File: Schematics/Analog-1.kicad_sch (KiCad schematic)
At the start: 65 parts, among them U23 TCA9548A, U24 MCP4728, U25 MCP4728, U26 MCP4728, U27 MCP4728, U28 MCP4728, U29 MCP4728, U30 MCP4728, U31 MCP4728, U32 MCP4728, U33 MCP4728, U34 MCP4728, U35 MCP4728, U36 MCP4728, U37 MCP4728, U38 MCP4728, U39 MCP4728, U40 TCA9548A, U41 LM1117-3.3, U42 MCP4728, U43 MCP4728, U44 MCP4728, U45 MCP4728, U46 MCP4728, U47 MCP4728, U48 TCA9548A

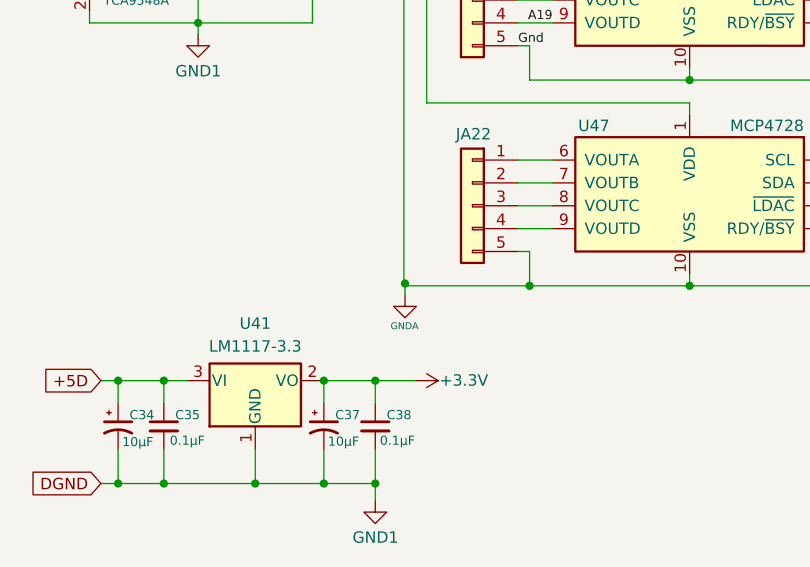
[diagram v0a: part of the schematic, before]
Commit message: Now with dual ESP32 with Midi32 and Disp32.
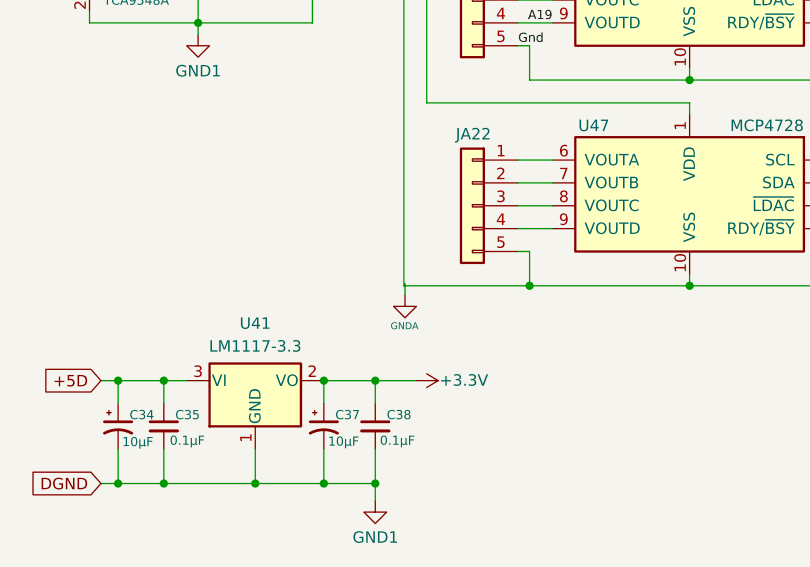
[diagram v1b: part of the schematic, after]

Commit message: Disp32 interface working properly.
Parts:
- renumbered R11 to R10, R5 to R4, R6 to R5, R7 to R6, R8 to R7, R9 to R8, R10 to R9
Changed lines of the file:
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@@
   (symbol (lib_id "Device:R_Small_US") (at 205.74 86.36 0) (mirror y) (unit 1)
     (in_bom yes) (on_board yes) (dnp no)
-    (property "Reference" "R6" (at 209.9411 84.455 0)
+    (property "Reference" "R5" (at 209.9411 84.455 0)
       (effects (font (size 1.016 1.016)) (justify left))
     )
@@
       (project "Schematics-Midi32"
         (path "/718f017d-28fe-4e29-b548-40db8e21cec7/5bc16b3a-a1cd-4002-8881-eefa1f194921"
-          (reference "R6") (unit 1)
+          (reference "R5") (unit 1)
         )
       )
@@
   (symbol (lib_id "Device:R_Small_US") (at 208.28 69.85 0) (mirror y) (unit 1)
     (in_bom yes) (on_board yes) (dnp no)
-    (property "Reference" "R7" (at 208.3796 67.9875 0)
+    (property "Reference" "R6" (at 208.3796 67.9875 0)
       (effects (font (size 1.016 1.016)) (justify right))
     )
@@
       (project "Schematics-Midi32"
         (path "/718f017d-28fe-4e29-b548-40db8e21cec7/5bc16b3a-a1cd-4002-8881-eefa1f194921"
-          (reference "R7") (unit 1)
+          (reference "R6") (unit 1)
         )
       )
@@
   (symbol (lib_id "Device:R_Small_US") (at 24.13 71.12 0) (unit 1)
     (in_bom yes) (on_board yes) (dnp no)
-    (property "Reference" "R5" (at 18.8695 69.2735 0)
+    (property "Reference" "R4" (at 18.8695 69.2735 0)
       (effects (font (size 1.27 1.27)) (justify left))
     )
@@
       (project "Schematics-Midi32"
         (path "/718f017d-28fe-4e29-b548-40db8e21cec7/5bc16b3a-a1cd-4002-8881-eefa1f194921"
-          (reference "R5") (unit 1)
+          (reference "R4") (unit 1)
         )
       )
@@
   (symbol (lib_id "Device:R_Small_US") (at 317.5 69.85 0) (mirror y) (unit 1)
     (in_bom yes) (on_board yes) (dnp no)
-    (property "Reference" "R10" (at 317.7079 67.884 0)
+    (property "Reference" "R9" (at 317.7079 67.884 0)
       (effects (font (size 1.016 1.016)) (justify right))
     )
@@
       (project "Schematics-Midi32"
         (path "/718f017d-28fe-4e29-b548-40db8e21cec7/5bc16b3a-a1cd-4002-8881-eefa1f194921"
-          (reference "R10") (unit 1)
+          (reference "R9") (unit 1)
         )
       )
@@
   (symbol (lib_id "Device:R_Small_US") (at 213.995 69.85 0) (mirror y) (unit 1)
     (in_bom yes) (on_board yes) (dnp no)
-    (property "Reference" "R8" (at 214.29 68.046 0)
+    (property "Reference" "R7" (at 214.29 68.046 0)
       (effects (font (size 1.016 1.016)) (justify right))
     )
@@
       (project "Schematics-Midi32"
         (path "/718f017d-28fe-4e29-b548-40db8e21cec7/5bc16b3a-a1cd-4002-8881-eefa1f194921"
-          (reference "R8") (unit 1)
+          (reference "R7") (unit 1)
         )
       )
@@
   (symbol (lib_id "Device:R_Small_US") (at 322.58 69.85 0) (mirror y) (unit 1)
     (in_bom yes) (on_board yes) (dnp no)
-    (property "Reference" "R11" (at 322.7405 67.9425 0)
+    (property "Reference" "R10" (at 322.7405 67.9425 0)
       (effects (font (size 1.016 1.016)) (justify right))
     )
@@
       (project "Schematics-Midi32"
         (path "/718f017d-28fe-4e29-b548-40db8e21cec7/5bc16b3a-a1cd-4002-8881-eefa1f194921"
-          (reference "R11") (unit 1)
+          (reference "R10") (unit 1)
         )
       )
@@
   (symbol (lib_id "Device:R_Small_US") (at 314.325 86.36 0) (mirror y) (unit 1)
     (in_bom yes) (on_board yes) (dnp no)
-    (property "Reference" "R9" (at 313.5122 84.2264 0)
+    (property "Reference" "R8" (at 313.5122 84.2264 0)
       (effects (font (size 1.016 1.016)) (justify left))
     )
@@
       (project "Schematics-Midi32"
         (path "/718f017d-28fe-4e29-b548-40db8e21cec7/5bc16b3a-a1cd-4002-8881-eefa1f194921"
-          (reference "R9") (unit 1)
-        )
-      )
+          (reference "R8") (unit 1)
+        )
+      )

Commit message: Noise generator and experimental steups.
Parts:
- added JS4: To Compute #1, symbol Connector_Generic:Conn_01x06
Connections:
- net +5D: now also JS4.1 (Pin_1), JS4.2 (Pin_2)
- net GND1: now also JS4.3 (Pin_3), JS4.6 (Pin_6)
- net at U48.1 (SC7): now also JS4.5 (Pin_5)
- net at U48.2 (SD7): now also JS4.4 (Pin_4)
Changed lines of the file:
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@@
   (junction (at 97.155 106.68) (diameter 0) (color 0 0 0 0)
   )
+  (junction (at 318.77 137.16) (diameter 0) (color 0 0 0 0)
+  )
   (junction (at 78.105 175.26) (diameter 0) (color 0 0 0 0)
   )
@@
   (junction (at 97.155 154.94) (diameter 0) (color 0 0 0 0)
   )
+  (junction (at 318.77 139.7) (diameter 0) (color 0 0 0 0)
+  )
   (junction (at 23.495 93.98) (diameter 0) (color 0 0 0 0)
   )
@@
     (stroke (width 0) (type default))
   )
+  (wire (pts (xy 290.83 116.84) (xy 292.735 116.84))
+    (stroke (width 0) (type default))
+  )
   (wire (pts (xy 78.105 152.4) (xy 97.155 152.4))
     (stroke (width 0) (type default))
@@
     (stroke (width 0) (type default))
   )
+  (wire (pts (xy 292.735 114.3) (xy 288.3662 114.3))
+    (stroke (width 0) (type default))
+  )
   (wire (pts (xy 55.245 49.53) (xy 55.245 71.12))
     (stroke (width 0) (type default))
@@
     (stroke (width 0) (type default))
   )
+  (wire (pts (xy 326.39 139.7) (xy 318.77 139.7))
+    (stroke (width 0) (type default))
+  )
   (wire (pts (xy 116.205 138.43) (xy 112.395 138.43))
     (stroke (width 0) (type default))
@@
     (stroke (width 0) (type default))
   )
+  (wire (pts (xy 318.77 139.7) (xy 306.07 139.7))
+    (stroke (width 0) (type default))
+  )
   (wire (pts (xy 260.985 129.54) (xy 278.13 129.54))
     (stroke (width 0) (type default))
@@
     (stroke (width 0) (type default))
   )
+  (wire (pts (xy 326.39 147.32) (xy 318.77 147.32))
+    (stroke (width 0) (type default))
+  )
   (wire (pts (xy 24.765 120.015) (xy 32.385 120.015))
     (stroke (width 0) (type default))
@@
     (stroke (width 0) (type default))
   )
+  (wire (pts (xy 318.77 137.16) (xy 318.77 134.62))
+    (stroke (width 0) (type default))
+  )
   (wire (pts (xy 172.085 92.71) (xy 166.37 92.71))
     (stroke (width 0) (type default))
@@
     (stroke (width 0) (type default))
   )
+  (wire (pts (xy 288.3662 144.78) (xy 326.39 144.78))
+    (stroke (width 0) (type default))
+  )
   (wire (pts (xy 132.08 189.23) (xy 135.89 189.23))
     (stroke (width 0) (type default))
@@
     (stroke (width 0) (type default))
   )
+  (wire (pts (xy 318.77 137.16) (xy 306.07 137.16))
+    (stroke (width 0) (type default))
+  )
   (wire (pts (xy 151.13 83.82) (xy 151.13 82.55))
     (stroke (width 0) (type default))
@@
     (stroke (width 0) (type default))
   )
+  (wire (pts (xy 290.83 142.24) (xy 326.39 142.24))
+    (stroke (width 0) (type default))
+  )
   (wire (pts (xy 243.205 34.29) (xy 243.205 38.1))
     (stroke (width 0) (type default))
@@
     (stroke (width 0) (type default))
   )
+  (wire (pts (xy 290.83 116.84) (xy 290.83 142.24))
+    (stroke (width 0) (type default))
+  )
   (wire (pts (xy 112.395 191.77) (xy 116.205 191.77))
     (stroke (width 0) (type default))
@@
     (stroke (width 0) (type default))
   )
+  (wire (pts (xy 326.39 137.16) (xy 318.77 137.16))
+    (stroke (width 0) (type default))
+  )
   (wire (pts (xy 26.67 137.16) (xy 33.02 137.16))
     (stroke (width 0) (type default))
@@
     (stroke (width 0) (type default))
   )
+  (wire (pts (xy 318.77 134.62) (xy 326.39 134.62))
+    (stroke (width 0) (type default))
+  )
   (wire (pts (xy 24.13 55.88) (xy 24.13 68.58))
     (stroke (width 0) (type default))
@@
     (stroke (width 0) (type default))
   )
+  (wire (pts (xy 318.77 147.32) (xy 318.77 139.7))
+    (stroke (width 0) (type default))
+  )
   (wire (pts (xy 97.155 63.5) (xy 151.13 63.5))
     (stroke (width 0) (type default))
@@
   )
   (wire (pts (xy 116.205 74.93) (xy 112.395 74.93))
+    (stroke (width 0) (type default))
+  )
+  (wire (pts (xy 288.3662 114.3) (xy 288.3662 144.78))
     (stroke (width 0) (type default))
   )
@@
     )
   )
+  (global_label "DGND" (shape output) (at 306.07 139.7 180) (fields_autoplaced)
+    (effects (font (size 1.27 1.27) italic) (justify right))
+    (property "Intersheetrefs" "${INTERSHEET_REFS}" (at 298.2608 139.6206 0)
+      (effects (font (size 1.27 1.27) italic) (justify right) hide)
+    )
+  )
   (global_label "AGND" (shape output) (at 36.83 149.86 0) (fields_autoplaced)
     (effects (font (size 1.27 1.27) italic) (justify left))
@@
     (property "Intersheetrefs" "${INTERSHEET_REFS}" (at 227.7308 78.6606 0)
       (effects (font (size 1.27 1.27) italic) (justify left) hide)
+    )
+  )
+  (global_label "+5D" (shape output) (at 306.07 137.16 180) (fields_autoplaced)
+    (effects (font (size 1.27 1.27) italic) (justify right))
+    (property "Intersheetrefs" "${INTERSHEET_REFS}" (at 299.3494 137.0806 0)
+      (effects (font (size 1.27 1.27) italic) (justify right) hide)
     )
   )
@@
         )
       )
+    )
+  )
+  (symbol (lib_id "Connector_Generic:Conn_01x06") (at 331.47 139.7 0) (unit 1)
+    (in_bom yes) (on_board yes) (dnp no)
+    (property "Reference" "JS4" (at 331.47 131.445 0)
+      (effects (font (size 1.27 1.27)))
+    )
+    (property "Value" "To Compute #1" (at 334.01 149.86 0)
+      (effects (font (size 0.762 0.762)) hide)
+    )
+    (property "Footprint" "" (at 331.47 139.7 0)
+      (effects (font (size 1.27 1.27)) hide)
+    )
+    (property "Datasheet" "~" (at 331.47 139.7 0)
+      (effects (font (size 1.27 1.27)) hide)
+    )
+    (pin "1")
+    (pin "2")
+    (pin "3")
+    (pin "4")
+    (pin "5")
+    (pin "6")
+    (instances
+      (project "Schematics-Midi32"
+        (path "/718f017d-28fe-4e29-b548-40db8e21cec7/5bc16b3a-a1cd-4002-8881-eefa1f194921"
+          (reference "JS4") (unit 1)
+        )
+      )
+      (project "Analog-52channel"
+        (path "/e36b28a4-7427-4708-a63e-3fe312e8d49f"
+          (reference "JS2") (unit 1)
+        )
+      )

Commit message: adding noise source and variable state filter.
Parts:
- renumbered C32 to C28, C33 to C29, C34 to C30, C35 to C31, C36 to C32, C37 to C33, C38 to C34, C39 to C35, JP3 to JP1, JS4 to JS2, U23 to U22, U24 to U23, U25 to U24, U26 to U25, U27 to U26, U28 to U27, U29 to U28, U30 to U29, U31 to U30, U32 to U31, U33 to U32, U34 to U33, U35 to U34, U36 to U35, U37 to U36, U38 to U37, U39 to U38, U40 to U39, U41 to U40, U42 to U41, U43 to U42, U44 to U43, U45 to U44, U46 to U45, U47 to U46, U48 to U47

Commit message: Partial software with complete hardware on best 3 state filter with 4 outputs.
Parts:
- renumbered C35 to C?, C34 to C?, C28 to C?, C31 to C?, C32 to C?, C29 to C?, C30 to C?, C33 to C?, JA16 to JA?, JA7 to JA?, JA9 to JA?, JA14 to JA?, JA20 to JA?, JA18 to JA?, JA19 to JA?, JA3 to JA?, JA2 to JA?, JA21 to JA?, JA8 to JA?, JA10 to JA?, JA6 to JA?, JA4 to JA?, JA17 to JA?, JA11 to JA?, JA5 to JA?, JA22 to JA?, JA15 to JA?, JA1 to JA?, JA12 to JA?, JA13 to JA?, JP1 to JP?, JS2 to JS?, JS1 to JS?, R5 to R?, R6 to R?, R4 to R?, R9 to R?, R7 to R?, R10 to R?, R8 to R?, U22 to U?, U30 to U?, U45 to U?, U43 to U?, U28 to U?, U42 to U?, U27 to U?, U40 to U?, U35 to U?, U26 to U?, U41 to U?, U38 to U?, U39 to U?, U34 to U?, U37 to U?, U23 to U?, U44 to U?, U46 to U?, U47 to U?, U32 to U?, U33 to U?, U36 to U?, U29 to U?, U24 to U?, U25 to U?, U31 to U?

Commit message: - Updated current libraries - New 7 inc display with ESP32S3 and second USB upload port - Start of I2C feeder interface slave on display.
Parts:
- gave numbers to parts that had none: 66

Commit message: updated schematics.
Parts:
- removed JS1: To Compute #1, symbol Connector_Generic:Conn_01x06
- removed R78, R79: 10k, symbol Device:R_Small_US
- added J13: Conn_01x03, symbol My Connectors:Conn_01x03
- added J14, J15: Conn_01x06, symbol My Connectors:Conn_01x06
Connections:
- net +5D: now also J14.5 (Pin_5), J14.6 (Pin_6), J15.1 (Pin_1), J15.2 (Pin_2)
- net GND1: now also J13.1 (Pin_1), J14.1 (Pin_1), J14.4 (Pin_4), J15.3 (Pin_3), J15.6 (Pin_6)
- net SCL0: now also J14.2 (Pin_2), J15.5 (Pin_5)
- net SDA0: now also J14.3 (Pin_3), J15.4 (Pin_4)
- net at U51.3 (SC6): now also J13.3 (Pin_3)
- net at U51.4 (SD6): now also J13.2 (Pin_2)
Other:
- note added: "From µProc"
- note added: "To Next Board"
- moved on the sheet: C76, JS2, R80, R81, R84, U51
